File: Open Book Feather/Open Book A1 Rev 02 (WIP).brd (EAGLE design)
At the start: 77.5 x 112.3 mm, 124 parts, among them J1 SJ-43514-SMT, J2 10118193-0001LF, Q1 DMG341, Q2 IRLML0100, SW1 SPDT_SWITCH, U1 AP2112-3.3, U2 MCP73831T-2ACI/OT, U3 ATSAMD51J64-TQFP(10X10), U4 GD25Q16C (or GD25Q32C), U5 74AC165D, U6 GD25Q16C (or GD25Q32C), U7 23K256-I/SN, U8 MAX4466EXK+T, X1 JSTPH, X2 2x5 0.05" SWD

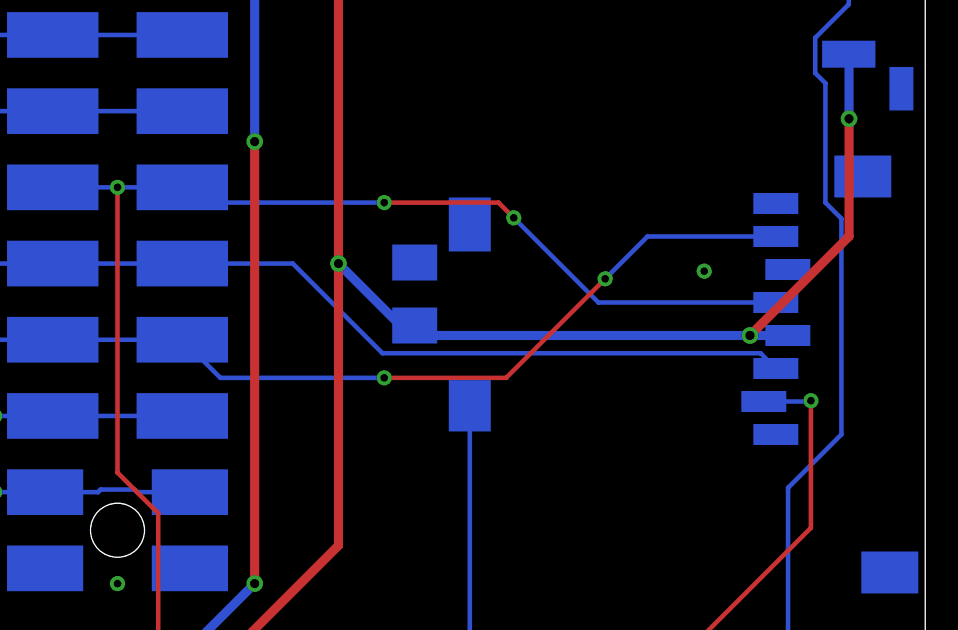
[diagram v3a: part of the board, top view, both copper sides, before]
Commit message: improve clearance around C24
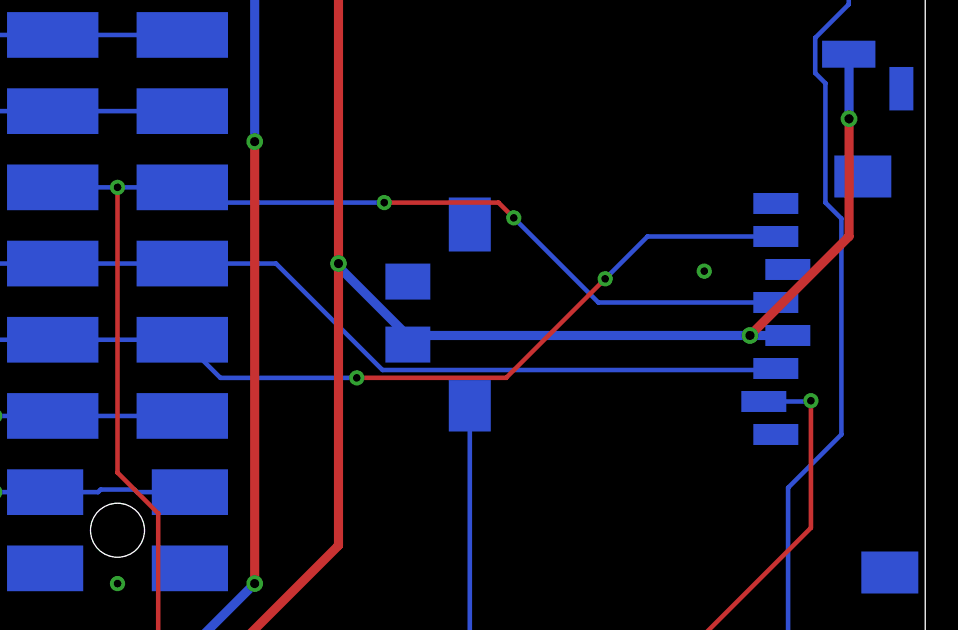
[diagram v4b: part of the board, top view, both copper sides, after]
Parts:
- moved C24 0.67 mm to (60.0, 76.3)
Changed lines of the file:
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@@
 <setting verticaltext="up"/>
 </settings>
-<grid distance="0.01" unitdist="inch" unit="inch" style="lines" multiple="1" display="no" altdistance="0.005" altunitdist="inch" altunit="inch"/>
+<grid distance="0.01" unitdist="inch" unit="inch" style="lines" multiple="1" display="no" altdistance="0.001" altunitdist="inch" altunit="inch"/>
 <layers>
-<layer number="1" name="Top" color="4" fill="1" visible="no" active="yes"/>
+<layer number="1" name="Top" color="4" fill="1" visible="yes" active="yes"/>
 <layer number="2" name="Route2" color="1" fill="3" visible="no" active="no"/>
 <layer number="3" name="Route3" color="4" fill="3" visible="no" active="no"/>
@@
 <layer number="14" name="Route14" color="1" fill="6" visible="no" active="no"/>
 <layer number="15" name="Route15" color="4" fill="6" visible="no" active="no"/>
-<layer number="16" name="Bottom" color="1" fill="1" visible="no" active="yes"/>
-<layer number="17" name="Pads" color="2" fill="1" visible="no" active="yes"/>
-<layer number="18" name="Vias" color="2" fill="1" visible="no" active="yes"/>
+<layer number="16" name="Bottom" color="1" fill="1" visible="yes" active="yes"/>
+<layer number="17" name="Pads" color="2" fill="1" visible="yes" active="yes"/>
+<layer number="18" name="Vias" color="2" fill="1" visible="yes" active="yes"/>
 <layer number="19" name="Unrouted" color="6" fill="1" visible="yes" active="yes"/>
 <layer number="20" name="Dimension" color="15" fill="1" visible="yes" active="yes"/>
-<layer number="21" name="tPlace" color="14" fill="1" visible="no" active="yes"/>
+<layer number="21" name="tPlace" color="14" fill="1" visible="yes" active="yes"/>
 <layer number="22" name="bPlace" color="13" fill="1" visible="yes" active="yes"/>
-<layer number="23" name="tOrigins" color="15" fill="1" visible="no" active="yes"/>
+<layer number="23" name="tOrigins" color="15" fill="1" visible="yes" active="yes"/>
 <layer number="24" name="bOrigins" color="15" fill="1" visible="yes" active="yes"/>
-<layer number="25" name="tNames" color="7" fill="1" visible="no" active="yes"/>
+<layer number="25" name="tNames" color="7" fill="1" visible="yes" active="yes"/>
 <layer number="26" name="bNames" color="7" fill="1" visible="yes" active="yes"/>
 <layer number="27" name="tValues" color="7" fill="1" visible="no" active="yes"/>
 <layer number="28" name="bValues" color="7" fill="1" visible="no" active="yes"/>
 <layer number="29" name="tStop" color="7" fill="3" visible="no" active="yes"/>
-<layer number="30" name="bStop" color="7" fill="6" visible="yes" active="yes"/>
+<layer number="30" name="bStop" color="7" fill="6" visible="no" active="yes"/>
 <layer number="31" name="tCream" color="7" fill="4" visible="no" active="yes"/>
 <layer number="32" name="bCream" color="7" fill="5" visible="no" active="yes"/>
@@
 <layer number="37" name="tTest" color="7" fill="1" visible="no" active="yes"/>
 <layer number="38" name="bTest" color="7" fill="1" visible="no" active="yes"/>
-<layer number="39" name="tKeepout" color="4" fill="11" visible="no" active="yes"/>
-<layer number="40" name="bKeepout" color="1" fill="11" visible="no" active="yes"/>
-<layer number="41" name="tRestrict" color="4" fill="10" visible="no" active="yes"/>
-<layer number="42" name="bRestrict" color="1" fill="10" visible="no" active="yes"/>
+<layer number="39" name="tKeepout" color="4" fill="11" visible="yes" active="yes"/>
+<layer number="40" name="bKeepout" color="1" fill="11" visible="yes" active="yes"/>
+<layer number="41" name="tRestrict" color="4" fill="10" visible="yes" active="yes"/>
+<layer number="42" name="bRestrict" color="1" fill="10" visible="yes" active="yes"/>
 <layer number="43" name="vRestrict" color="2" fill="10" visible="no" active="yes"/>
 <layer number="44" name="Drills" color="7" fill="1" visible="no" active="yes"/>
@@
 <layer number="49" name="Reference" color="7" fill="1" visible="no" active="yes"/>
 <layer number="50" name="dxf" color="7" fill="1" visible="no" active="yes"/>
-<layer number="51" name="tDocu" color="7" fill="1" visible="no" active="yes"/>
+<layer number="51" name="tDocu" color="7" fill="1" visible="yes" active="yes"/>
 <layer number="52" name="bDocu" color="7" fill="1" visible="yes" active="yes"/>
 <layer number="53" name="tGND_GNDA" color="7" fill="9" visible="no" active="no"/>
@@
 <attribute name="VALUE" x="13.208" y="67.691" size="0.508" layer="28" font="vector" ratio="18" rot="MR270" align="center"/>
 </element>
-<element name="C24" library="microbuilder" package="0805_10MGAP" value="10uF" x="60.198" y="76.962" smashed="yes" rot="MR90">
-<attribute name="NAME" x="59.055" y="76.962" size="0.508" layer="26" font="vector" ratio="18" rot="MR270" align="center"/>
-<attribute name="VALUE" x="61.468" y="76.962" size="0.508" layer="28" font="vector" ratio="18" rot="MR90" align="center"/>
+<element name="C24" library="microbuilder" package="0805_10MGAP" value="10uF" x="59.9694" y="76.327" smashed="yes" rot="MR90">
+<attribute name="NAME" x="58.8264" y="76.327" size="0.508" layer="26" font="vector" ratio="18" rot="MR270" align="center"/>
+<attribute name="VALUE" x="61.2394" y="76.327" size="0.508" layer="28" font="vector" ratio="18" rot="MR90" align="center"/>
 </element>
 <element name="C25" library="microbuilder" package="0805_10MGAP" value="1uF" x="24.384" y="12.954" smashed="yes" rot="MR180">
@@
 <wire x1="55.245" y1="28.134" x2="55.245" y2="29.337" width="0.1524" layer="16"/>
 <wire x1="55.245" y1="29.337" x2="53.6194" y2="30.9626" width="0.1524" layer="16"/>
-<wire x1="72.235" y1="74.48" x2="71.727" y2="74.988" width="0.1524" layer="16"/>
-<wire x1="71.727" y1="74.988" x2="59.124" y2="74.988" width="0.1524" layer="16"/>
-<wire x1="59.124" y1="74.988" x2="56.134" y2="77.978" width="0.1524" layer="16"/>
-<wire x1="56.134" y1="77.978" x2="52.451" y2="77.978" width="0.1524" layer="16"/>
+<wire x1="55.5752" y1="77.978" x2="52.451" y2="77.978" width="0.1524" layer="16"/>
 <wire x1="35.612" y1="55.738" x2="35.612" y2="57.3407125" width="0.1524" layer="16"/>
 <wire x1="35.612" y1="57.3407125" x2="35.8576" y2="57.5863125" width="0.1524" layer="16"/>
@@
 <contactref element="MS1" pad="12"/>
 <contactref element="MS1" pad="12'"/>
+<wire x1="72.235" y1="74.48" x2="72.1842" y2="74.4292" width="0.1524" layer="16"/>
+<wire x1="72.1842" y1="74.4292" x2="59.124" y2="74.4292" width="0.1524" layer="16"/>
+<wire x1="59.124" y1="74.4292" x2="55.5752" y2="77.978" width="0.1524" layer="16"/>
 </signal>
 <signal name="MISO">
@@
 <via x="66.548" y="77.47" extent="1-16" drill="0.254"/>
 <wire x1="66.548" y1="77.47" x2="63.246" y2="74.168" width="0.1524" layer="1"/>
-<wire x1="63.246" y1="74.168" x2="59.182" y2="74.168" width="0.1524" layer="1"/>
-<via x="59.182" y="74.168" extent="1-16" drill="0.254"/>
+<wire x1="63.246" y1="74.168" x2="58.2676" y2="74.168" width="0.1524" layer="1"/>
+<via x="58.2676" y="74.168" extent="1-16" drill="0.254"/>
 <wire x1="52.451" y1="75.438" x2="53.721" y2="74.168" width="0.1524" layer="16"/>
-<wire x1="59.182" y1="74.168" x2="53.721" y2="74.168" width="0.1524" layer="16"/>
+<wire x1="58.2676" y1="74.168" x2="53.721" y2="74.168" width="0.1524" layer="16"/>
 <via x="35.8068" y="64.77" extent="1-16" drill="0.254"/>
 <wire x1="35.112" y1="55.738" x2="35.112" y2="57.1607125" width="0.1524" layer="16"/>
@@
 <contactref element="C28" pad="1"/>
 <via x="57.658" y="77.978" extent="1-16" drill="0.3048"/>
-<wire x1="57.658" y1="77.978" x2="59.724" y2="75.912" width="0.3048" layer="16"/>
-<wire x1="59.724" y1="75.912" x2="60.198" y2="75.912" width="0.3048" layer="16"/>
+<wire x1="57.658" y1="77.978" x2="57.658" y2="77.8764" width="0.3048" layer="16"/>
+<wire x1="59.9694" y1="75.565" x2="57.658" y2="77.8764" width="0.3048" layer="16"/>
+<wire x1="59.9694" y1="75.565" x2="59.9694" y2="75.277" width="0.3048" layer="16"/>
 <wire x1="57.658" y1="77.978" x2="57.658" y2="68.58" width="0.3048" layer="1"/>
 <wire x1="57.658" y1="68.58" x2="53.721" y2="64.643" width="0.3048" layer="1"/>
@@
 <wire x1="31.75" y1="46.788" x2="34.798" y2="46.788" width="0.3048" layer="1"/>
 <wire x1="72.635" y1="75.58" x2="71.374" y2="75.58" width="0.3048" layer="16"/>
-<wire x1="71.374" y1="75.58" x2="60.53" y2="75.58" width="0.3048" layer="16"/>
-<wire x1="60.53" y1="75.58" x2="60.198" y2="75.912" width="0.3048" layer="16"/>
+<wire x1="71.374" y1="75.58" x2="60.2724" y2="75.58" width="0.3048" layer="16"/>
+<wire x1="60.2724" y1="75.58" x2="59.9694" y2="75.277" width="0.3048" layer="16"/>
 <wire x1="13.462" y1="94.234" x2="14.224" y2="93.472" width="0.3048" layer="1"/>
 <wire x1="34.798" y1="46.788" x2="37.794" y2="49.784" width="0.3048" layer="16"/>
